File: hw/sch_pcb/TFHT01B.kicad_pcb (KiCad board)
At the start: 2 copper layers, 30 x 15 mm, 31 parts, among them J1 SM04B-GHS-TB, J2 SM04B-GHS-TB, M1 M3, M2 M3, M3 M3, M4 M3, M5 M3, M6 M3, M7 CAP-SF2, Q1 BC817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

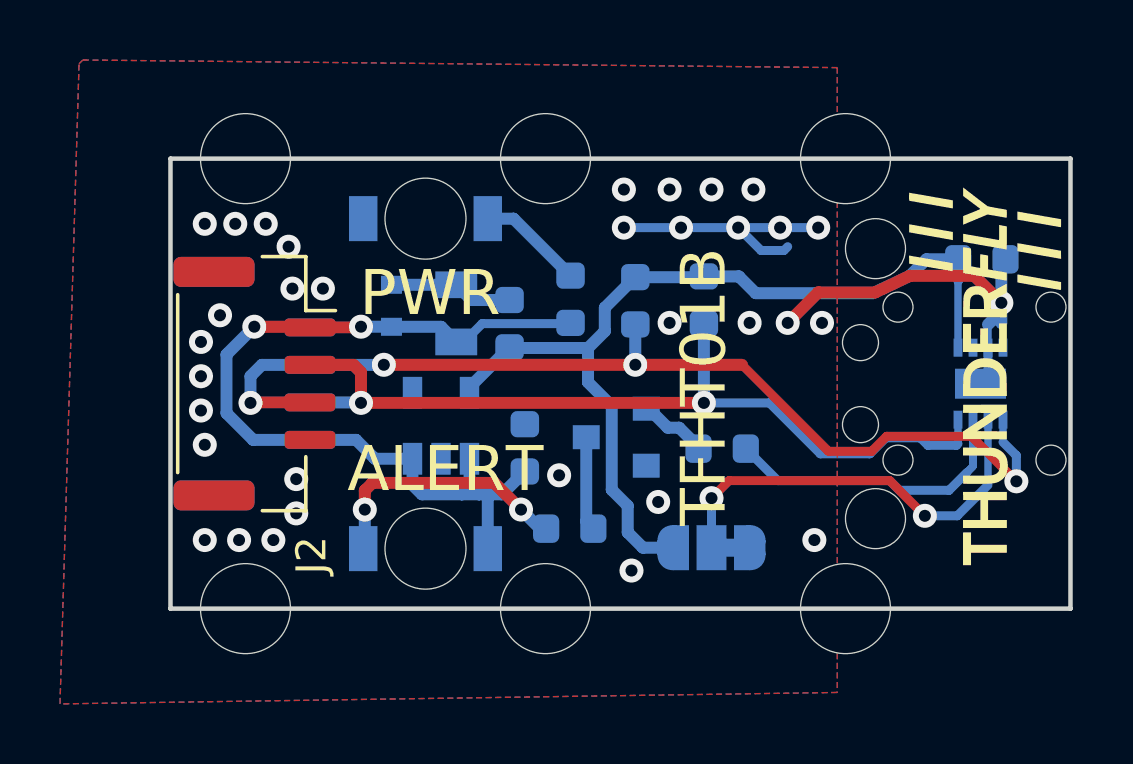
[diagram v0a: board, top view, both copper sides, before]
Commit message: Shift sensor to the center of the cap.
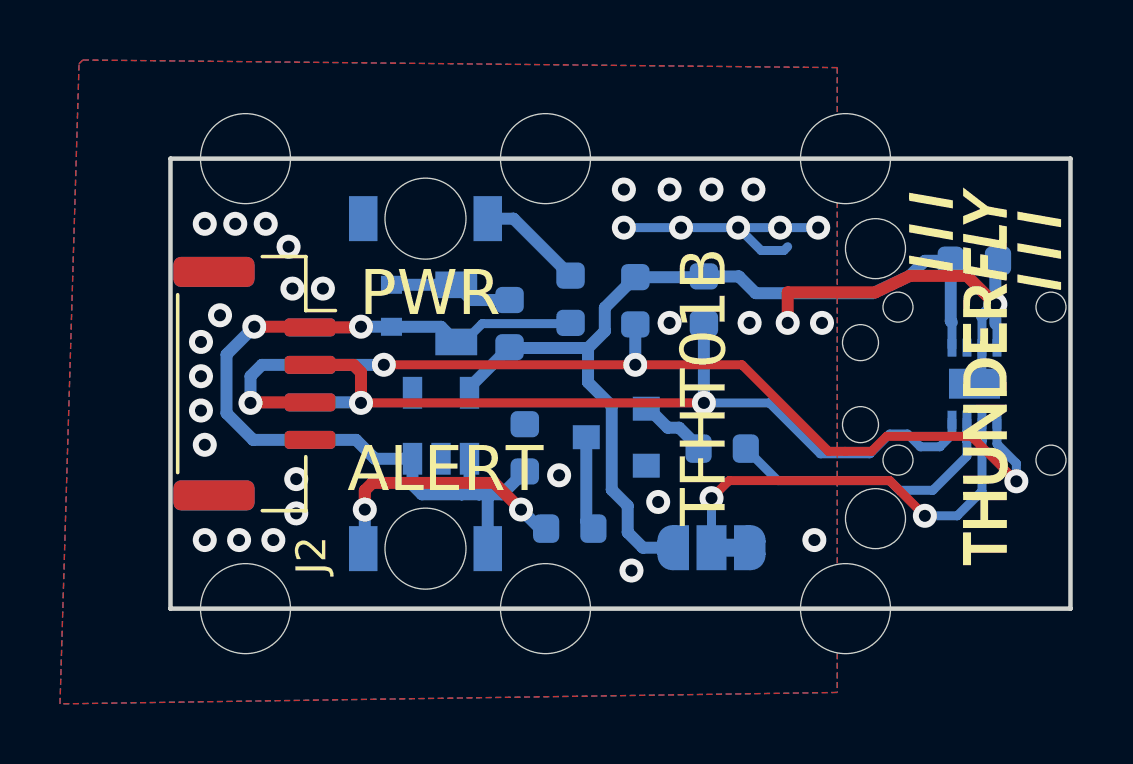
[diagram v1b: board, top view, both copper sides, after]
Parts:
- moved C5 0.25 mm to (26.8, -11.6)
- moved U1 0.20 mm to (26.8, -7.50)
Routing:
- net /ALERT: track 12.0 -> 9.76 mm

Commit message: Update value of base resistor #7. Generate manufacturing outputs.
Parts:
- R2: value 100R -> 10k
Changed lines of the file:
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@@
       (effects (font (size 1 1) (thickness 0.15)) (justify mirror))
     )
-    (fp_text value "100R" (at 0 -1.43) (layer "B.Fab") hide
+    (fp_text value "10k" (at 0 -1.43) (layer "B.Fab") hide
       (effects (font (size 1 1) (thickness 0.15)) (justify mirror))
     )
